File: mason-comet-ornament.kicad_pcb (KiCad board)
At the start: 2 copper layers, 95 x 53.6 mm, 10 parts, among them SW1 SW_SPDT

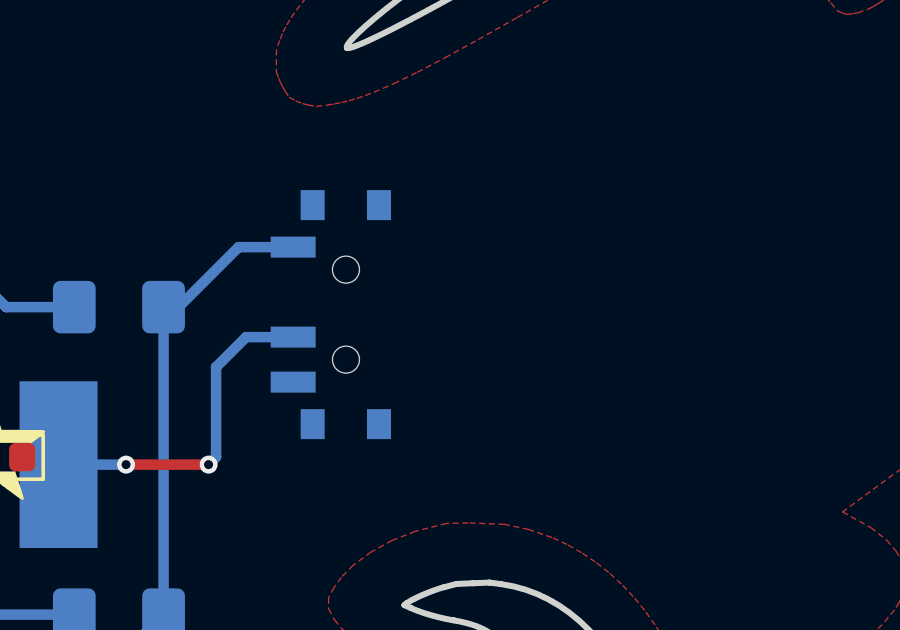
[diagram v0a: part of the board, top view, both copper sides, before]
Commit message: Added second power access
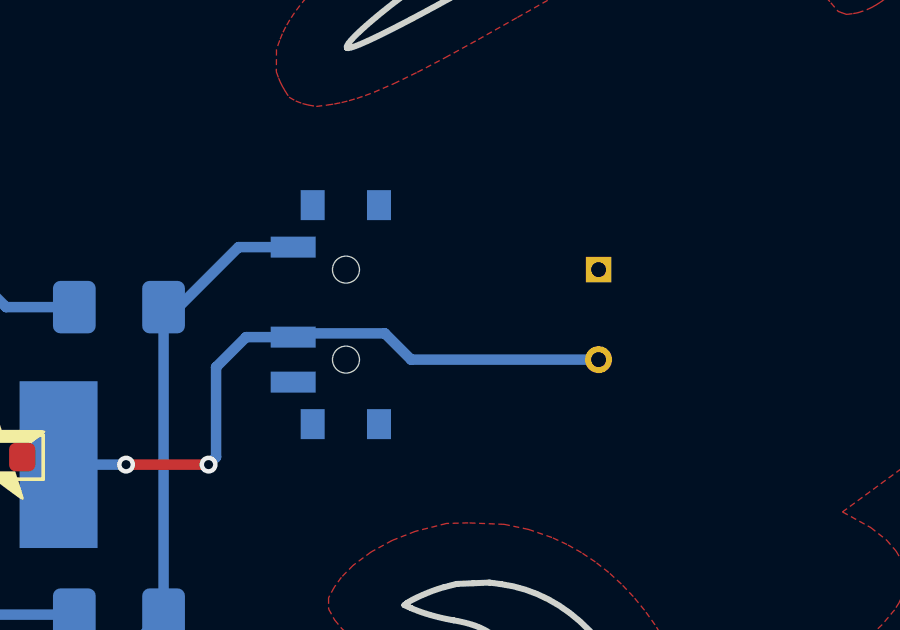
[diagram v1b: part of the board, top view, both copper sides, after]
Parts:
- added J1: Conn_01x01_Pin, Connector_PinHeader_1.00mm:PinHeader_1x01_P1.00mm_Vertical, F.Cu at (75.0, 46.0)
- added J2: Conn_01x01_Pin, Connector_PinHeader_1.00mm:PinHeader_1x01_P1.00mm_Vertical, F.Cu at (75.0, 43.0)
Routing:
- net Net-(BT1-+): track 11.3 -> 21.9 mm
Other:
- board text added: "3-5V"
- board text added: "GND"

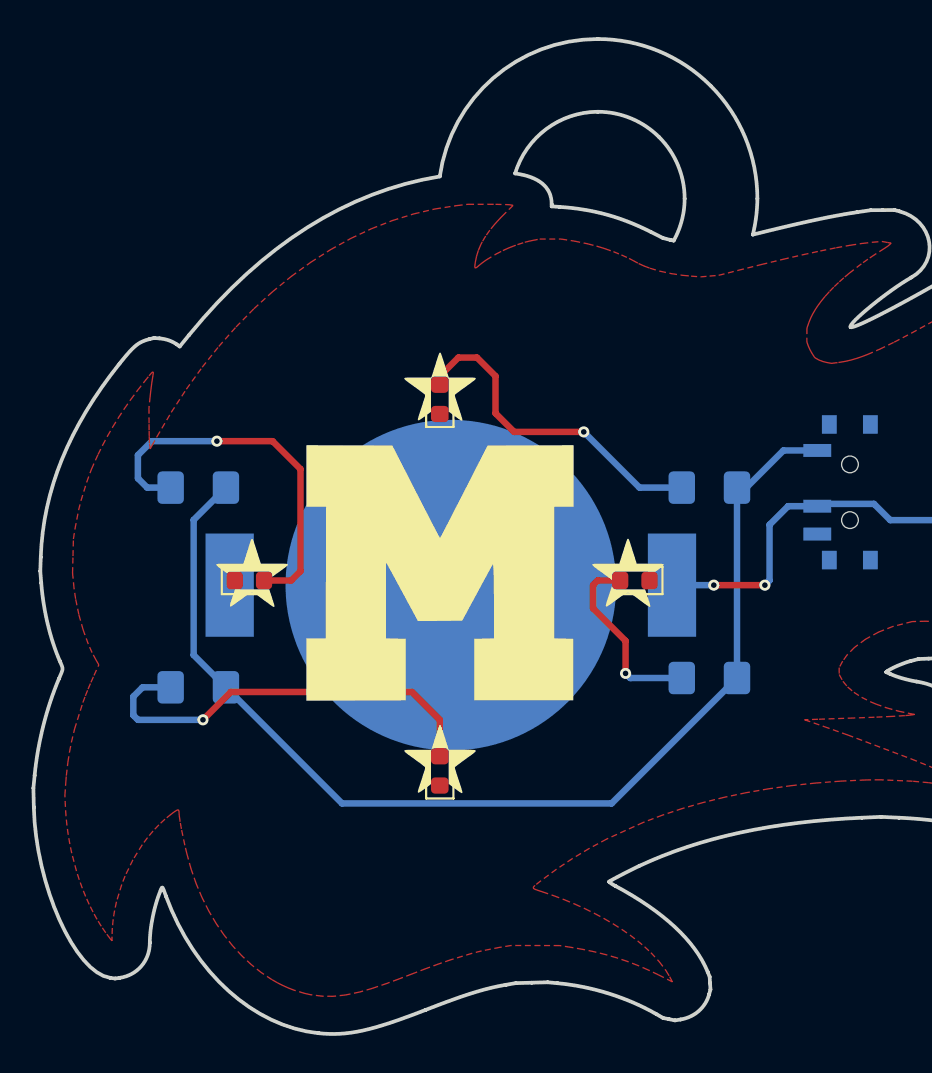
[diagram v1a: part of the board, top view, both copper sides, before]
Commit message: aliged with digikey parts/ordering
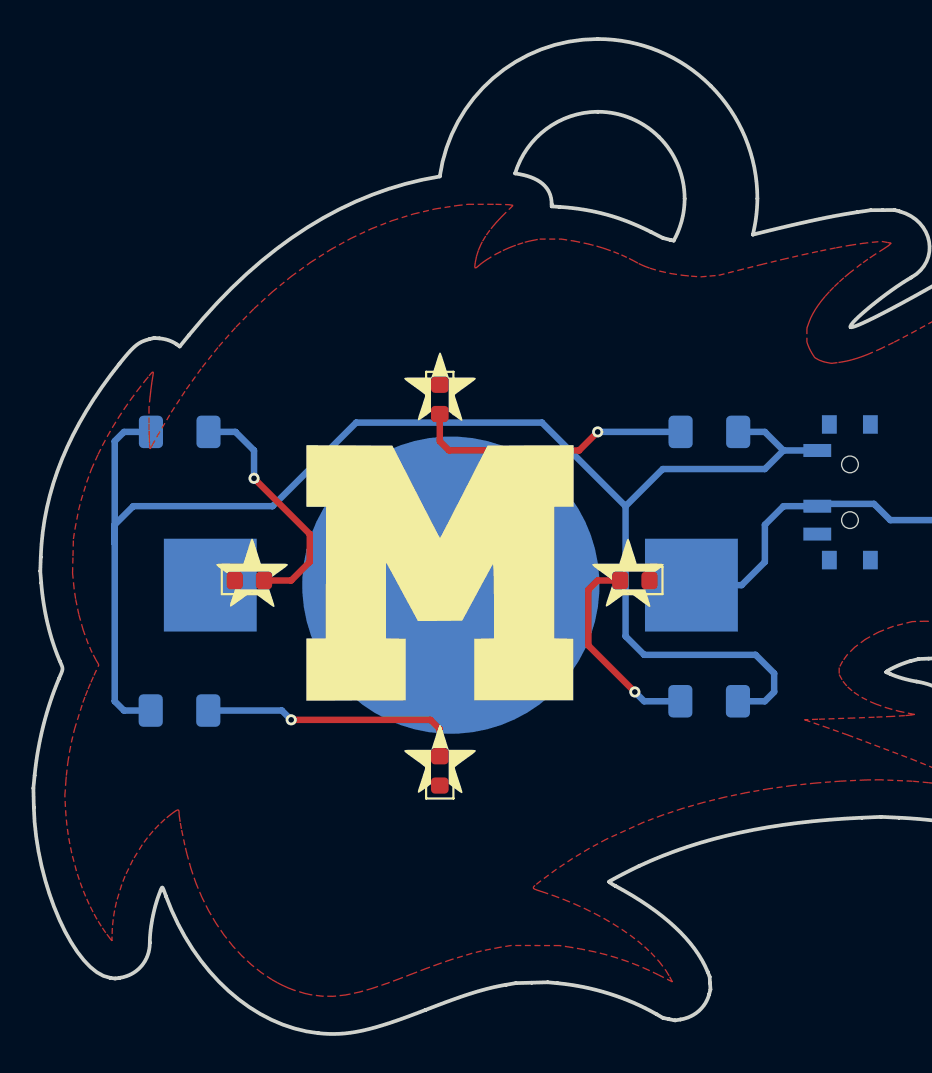
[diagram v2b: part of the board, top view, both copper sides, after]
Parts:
- BT1: footprint Battery:BatteryHolder_MPD_BC2003_1x2032 -> Battery:BatteryHolder_Multicomp_BC-2001_1x2032
- R1, R2, R3, R4: footprint LED_SMD:LED_1206_3216Metric_Pad1.42x1.75mm_HandSolder -> Resistor_SMD:R_1206_3216Metric_Pad1.30x1.75mm_HandSolder
- moved R2 3.16 mm to (30.5, 41.2), turned to 0 degrees
- moved R1 3.00 mm to (59.0, 41.2)
- moved R4 1.61 mm to (30.5, 56.2), turned to 0 degrees
- moved R3 1.25 mm to (59.0, 55.8)
- turned BT1 to 0 degrees
- turned D1 to -90 degrees
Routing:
- net Net-(SW1-A): track 60.5 -> 84.4 mm
- net Net-(D4-A): track 23.0 -> 14.3 mm
- net Net-(D2-A): track 20.6 -> 13.0 mm
- net Net-(D1-A): track 18.0 -> 15.1 mm
- net Net-(D3-A): track 10.2 -> 11.1 mm
- net Net-(BT1-+): track 21.9 -> 22.6 mm, vias 2 -> 0
- net GND: vias 0 -> 3
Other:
- board text added: "Applied Technology"
- board text added: "CR2032 Battery"
- board text added: "Corey Rice"
- board text added: "December 2024"
- board text added: "Mason, Ohio, USA"
- board text added: "Wm. Mason High School"
- board text added: "mason-comet-ornament"
- board text added: "v1.0.0"

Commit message: release version
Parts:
- D1, D2, D3, D4: footprint Diode_SMD:D_0603_1608Metric -> LED_SMD:LED_0603_1608Metric_Pad1.05x0.95mm_HandSolder
- moved J1 8.50 mm to (66.5, 46.0)
- moved J2 8.50 mm to (66.5, 43.0)
- moved SW1 7.72 mm to (74.0, 44.5)
- moved D3 0.40 mm to (54.6, 49.0)
- moved D1 0.40 mm to (44.5, 39.1)
- moved D4 0.40 mm to (44.5, 59.1)
- moved D2 0.20 mm to (34.4, 49.1)
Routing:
- net Net-(SW1-A): track 84.4 -> 93.0 mm
- net Net-(BT1-+): track 22.6 -> 18.5 mm
- net Net-(D2-A): track 13.0 -> 12.5 mm

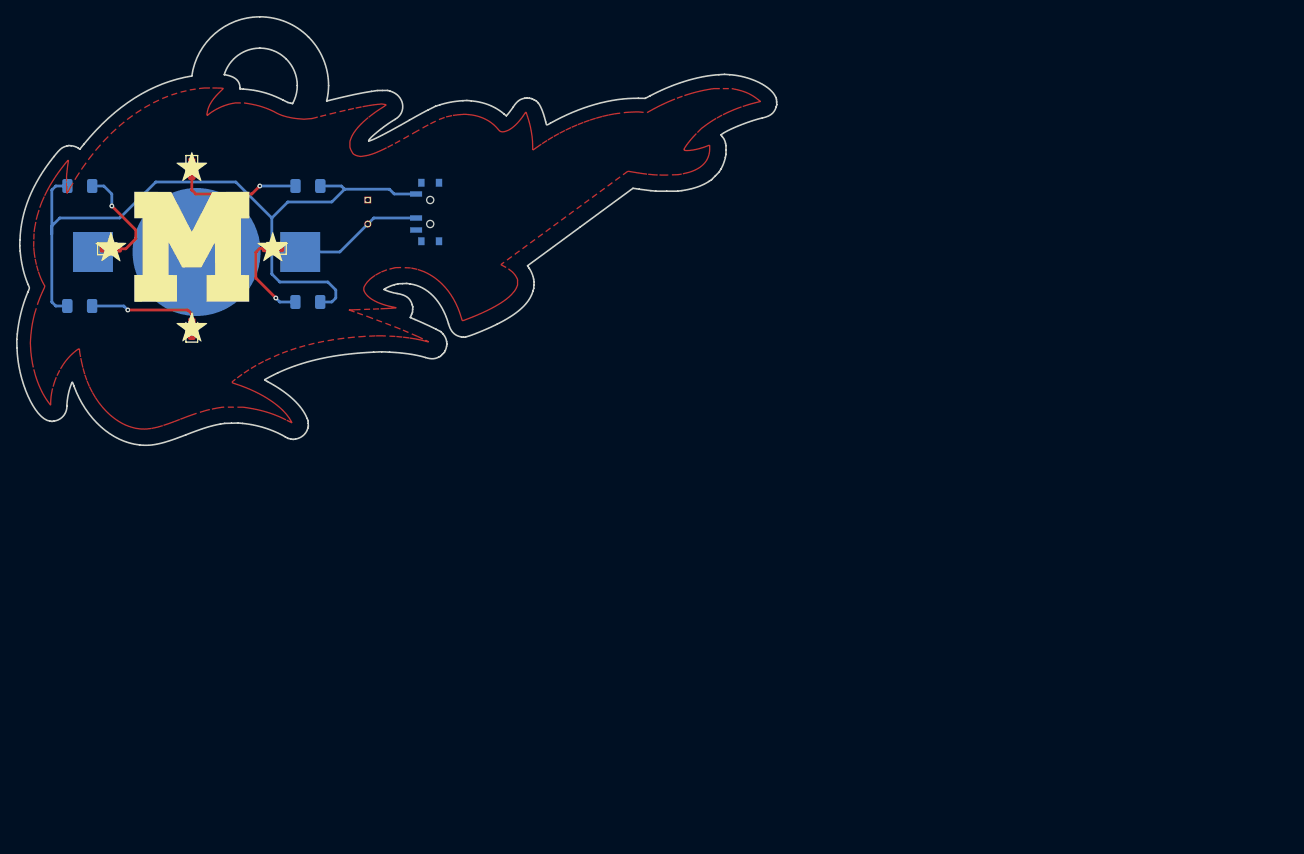
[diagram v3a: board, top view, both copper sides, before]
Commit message: updated sheet notes
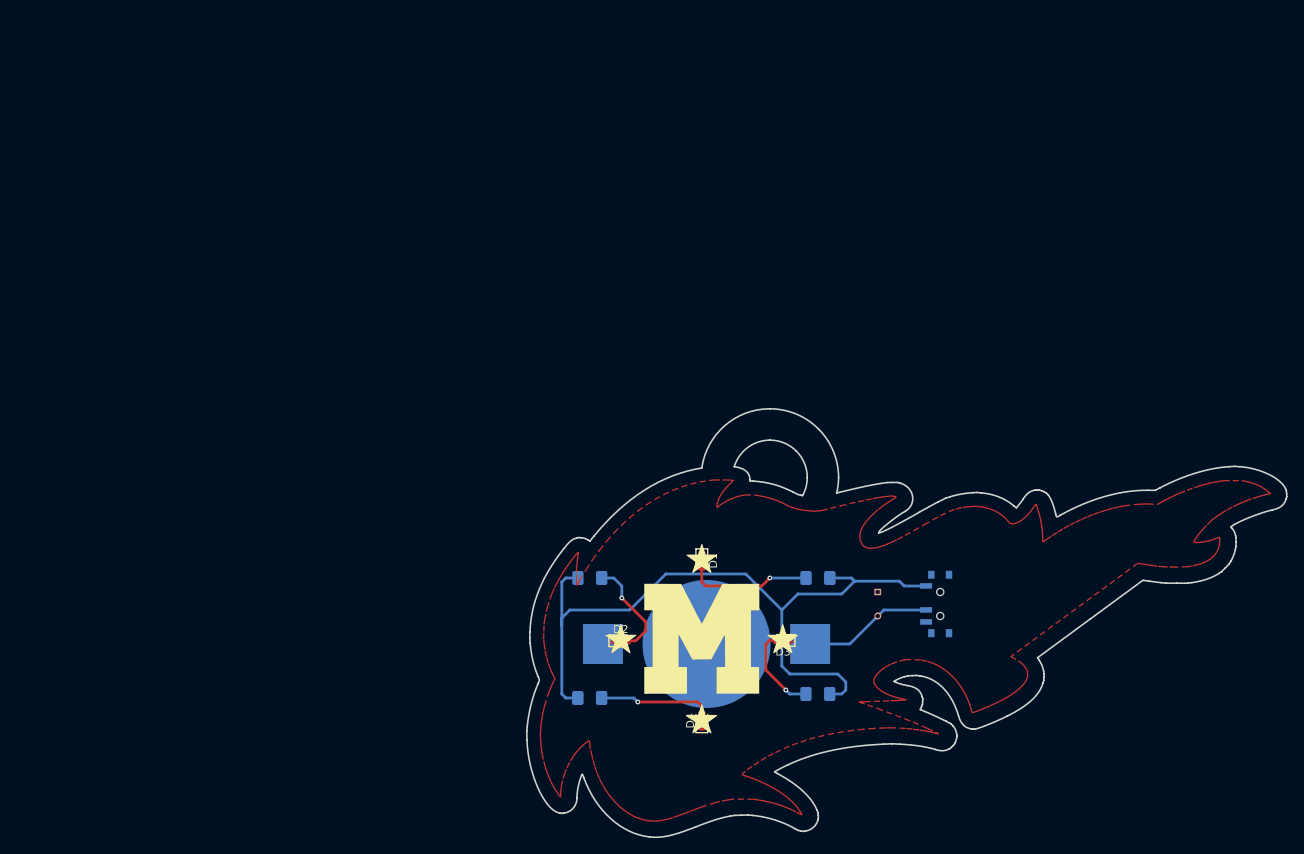
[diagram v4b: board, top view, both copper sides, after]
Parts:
- D1, D2, D3, D4: footprint LED_SMD:LED_0603_1608Metric_Pad1.05x0.95mm_HandSolder -> Diode_SMD:D_0603_1608Metric
- R1, R2, R3, R4: value R_US -> 1k; footprint Resistor_SMD:R_1206_3216Metric_Pad1.30x1.75mm_HandSolder -> LED_SMD:LED_1206_3216Metric_Pad1.42x1.75mm_HandSolder
- moved D3 80.4 mm to (118.4, 98.0)
- moved BT1 80.4 mm to (108.8, 98.5)
- moved D1 80.4 mm to (108.2, 88.1)
- moved D2 80.4 mm to (98.1, 98.1)
- moved D4 80.4 mm to (108.2, 108.1)
- moved J1 80.4 mm to (130.2, 95.0)
- moved J2 80.4 mm to (130.2, 92.0)
- moved R1 80.4 mm to (122.8, 90.2)
- moved R2 80.4 mm to (94.2, 90.2)
- moved R3 80.4 mm to (122.8, 104.8)
- moved R4 80.4 mm to (94.2, 105.2)
- moved SW1 80.4 mm to (137.7, 93.5)
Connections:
- net Net-(BT1-+) renamed VCC
